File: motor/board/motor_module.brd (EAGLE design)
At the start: 44.4 x 51.7 mm, 74 parts, among them IC6 LTC6088, IC7 DRV8833RTY

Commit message: Added parallel pull-up to status
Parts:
- added R39: 4.7k, biomimetic:0402-RES
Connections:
- net SWD_DIO/STATUS: now also R39.1
- net V_3.0: now also R39.2
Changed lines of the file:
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@@
 <element name="R38" library="biomimetic" package="0402-RES" value="4.7k" x="20.32" y="10.16" rot="R180"/>
 <element name="C11" library="biomimetic" package="0402-CAP" value="100nF" x="10.16" y="29.21" rot="R270"/>
+<element name="R39" library="biomimetic" package="0402-RES" value="4.7k" x="-8.89" y="-3.81"/>
 </elements>
 <signals>
@@
 <contactref element="IC6" pad="4"/>
 <contactref element="C29" pad="1"/>
+<contactref element="R39" pad="2"/>
 <wire x1="27.94" y1="27.1526" x2="30.2" y2="26.92" width="0" layer="19" extent="1-1"/>
 <wire x1="30.23" y1="11.92" x2="30.2" y2="26.92" width="0" layer="19" extent="1-1"/>
@@
 <wire x1="8.47" y1="31.13" x2="8.4074" y2="20.32" width="0" layer="19" extent="1-1"/>
 <wire x1="10.16" y1="32.2326" x2="8.47" y2="31.13" width="0" layer="19" extent="1-1"/>
+<wire x1="-8.4074" y1="-3.81" x2="12.2174" y2="1.27" width="0" layer="19" extent="1-1"/>
 </signal>
 <signal name="V_1.5">
@@
 <contactref element="U$20" pad="24"/>
 <contactref element="STATUS_LED" pad="C"/>
+<contactref element="R39" pad="1"/>
 <wire x1="23.61" y1="8.89" x2="28.43" y2="12.72" width="0" layer="19" extent="1-1"/>
+<wire x1="-9.3726" y1="-3.81" x2="23.61" y2="8.89" width="0" layer="19" extent="1-1"/>
 </signal>
 <signal name="I2C_SCL">

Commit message: Moved pullup on charge management status to vbus
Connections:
- net V_3.0: no longer R6.1
- net V_BUS: now also R6.1
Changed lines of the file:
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@@
 <contactref element="C1" pad="1"/>
 <contactref element="U$1" pad="6"/>
-<wire x1="14.72" y1="7.62" x2="19.8374" y2="3.81" width="0" layer="19" extent="1-1"/>
-<wire x1="13.22" y1="7.62" x2="14.72" y2="7.62" width="0" layer="19" extent="1-1"/>
-<wire x1="11.43" y1="8.1026" x2="13.22" y2="7.62" width="0" layer="19" extent="1-1"/>
+<contactref element="R6" pad="1"/>
+<wire x1="6.67" y1="15.204" x2="8.4074" y2="20.32" width="0" layer="19" extent="1-1"/>
+<wire x1="5.8674" y1="12.7" x2="6.67" y2="15.204" width="0" layer="19" extent="1-1"/>
+<wire x1="2.54" y1="16.18" x2="6.67" y2="15.204" width="0" layer="19" extent="1-1"/>
+<wire x1="11.43" y1="8.1026" x2="5.8674" y2="12.7" width="0" layer="19" extent="1-1"/>
+<wire x1="13.22" y1="7.62" x2="11.43" y2="8.1026" width="0" layer="19" extent="1-1"/>
+<wire x1="14.72" y1="7.62" x2="13.22" y2="7.62" width="0" layer="19" extent="1-1"/>
 <wire x1="6.35" y1="4.81" x2="11.43" y2="8.1026" width="0" layer="19" extent="1-1"/>
-<wire x1="5.8674" y1="12.7" x2="11.43" y2="8.1026" width="0" layer="19" extent="1-1"/>
-<wire x1="6.67" y1="15.204" x2="5.8674" y2="12.7" width="0" layer="19" extent="1-1"/>
-<wire x1="2.54" y1="16.18" x2="6.67" y2="15.204" width="0" layer="19" extent="1-1"/>
+<wire x1="19.8374" y1="3.81" x2="14.72" y2="7.62" width="0" layer="19" extent="1-1"/>
 </signal>
 <signal name="N$4">
@@
 </signal>
 <signal name="V_3.0">
-<contactref element="R6" pad="1"/>
 <contactref element="C2" pad="1"/>
 <contactref element="U$11" pad="3"/>
@@
 <wire x1="13.4874" y1="3.81" x2="12.2174" y2="5.08" width="0" layer="19" extent="1-1"/>
 <wire x1="12.2174" y1="1.27" x2="13.4874" y2="3.81" width="0" layer="19" extent="1-1"/>
-<wire x1="8.4074" y1="20.32" x2="13.22" y2="7.22" width="0" layer="19" extent="1-1"/>
-<wire x1="8.47" y1="31.13" x2="8.4074" y2="20.32" width="0" layer="19" extent="1-1"/>
-<wire x1="10.16" y1="32.2326" x2="8.47" y2="31.13" width="0" layer="19" extent="1-1"/>
+<wire x1="10.16" y1="32.2326" x2="27.94" y2="27.1526" width="0" layer="19" extent="1-1"/>
+<wire x1="8.47" y1="31.13" x2="10.16" y2="32.2326" width="0" layer="19" extent="1-1"/>
 <wire x1="-8.4074" y1="-3.81" x2="12.2174" y2="1.27" width="0" layer="19" extent="1-1"/>
 </signal>

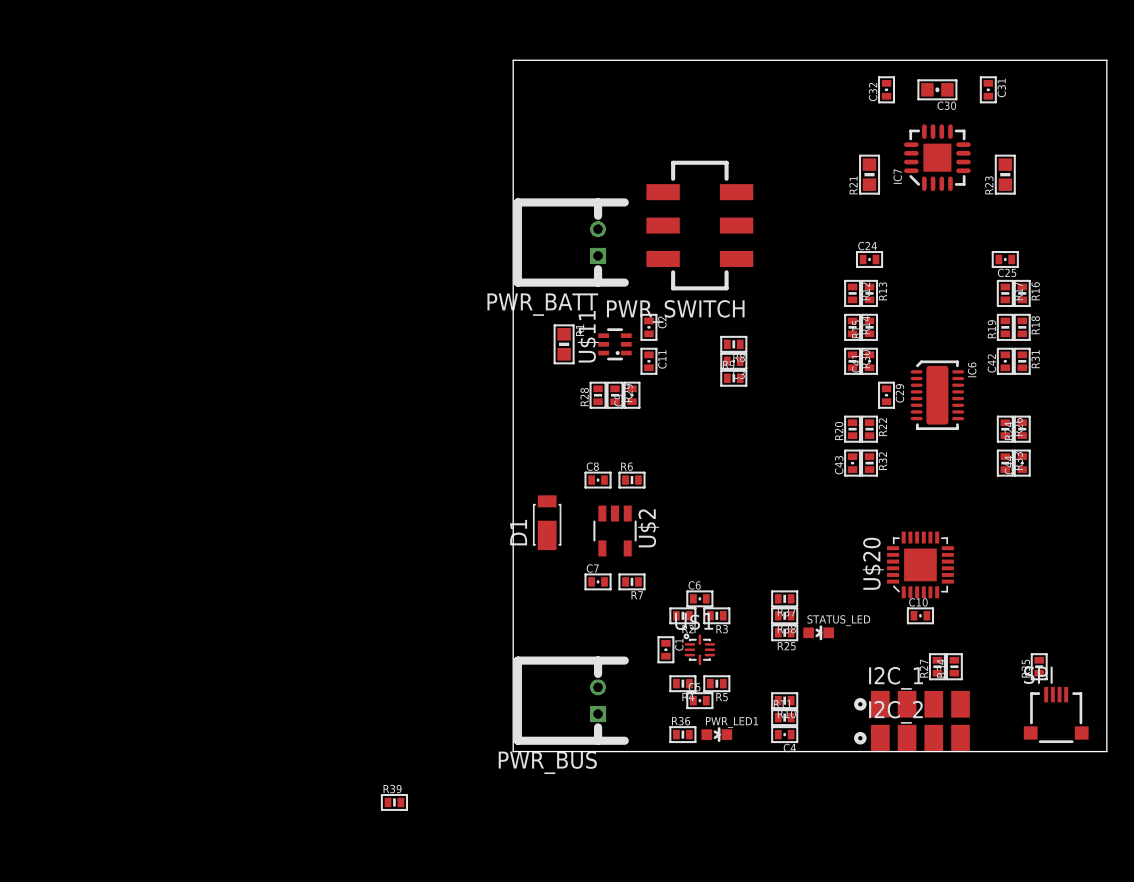
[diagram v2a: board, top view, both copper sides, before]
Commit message: Working on motor layout for modular motor driver
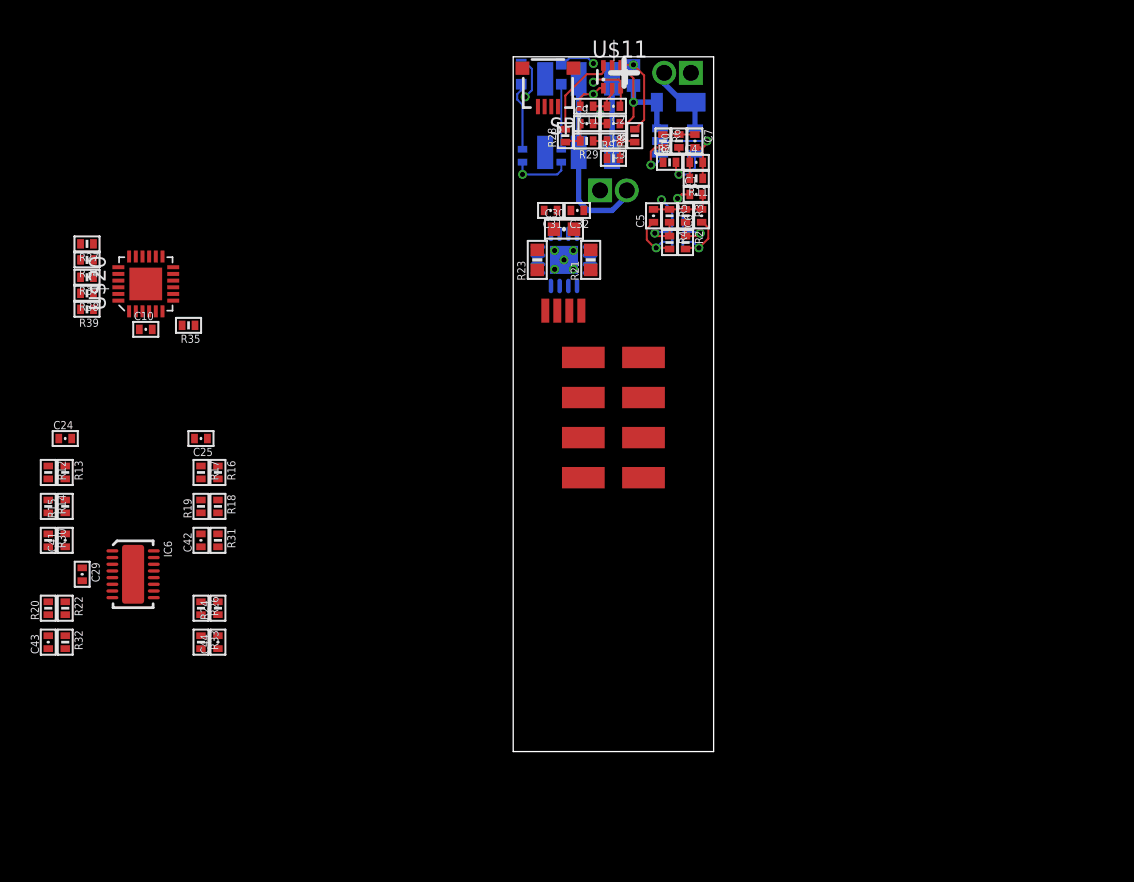
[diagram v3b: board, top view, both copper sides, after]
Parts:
- removed I2C_1, I2C_2: (no value), modular_robotics:1X04_2MM_BOARDEDGE
- added MA1, MA2, MB1, MB2: PAD-0.6_1.8, modular_robotics:PAD_0.6_1.8
- added U$27: MOTOR_HOUSING, modular_robotics:MOTOR_HOUSING
- PWR_BATT, PWR_BUS: value JST-RCY-FEMALE -> JST-RCY-FEMALEBATTERY; device modular_robotics:JST_2_FEMALE -> modular_robotics:TP_LIPO_160MAH
- moved R34 71.7 mm to (-31.9, 36.8), turned to 180 degrees
- moved R27 71.1 mm to (-31.9, 38.0), turned to 180 degrees
- moved R35 68.6 mm to (-24.3, 31.9), turned to 180 degrees
- moved C10 61.8 mm to (-27.5, 31.6)
- moved U$20 61.7 mm to (-27.5, 35.0)
- moved C24 61.7 mm to (-33.5, 23.4)
- moved C25 61.7 mm to (-23.4, 23.4)
- moved C29 61.7 mm to (-32.3, 13.3)
- moved C41 61.7 mm to (-33.5, 15.8)
- moved C42 61.7 mm to (-23.4, 15.8)
- moved C44 61.7 mm to (-22.1, 8.19)
- moved IC6 61.7 mm to (-28.4, 13.3)
- moved R13 61.7 mm to (-33.5, 20.9)
- moved R15 61.7 mm to (-33.5, 18.4)
- moved R16 61.7 mm to (-22.1, 20.9)
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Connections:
- net GND: now also PWR_BATT.V-, PWR_BUS.V-, U$27.2, U$27.6; no longer I2C_1.2, I2C_2.2, PWR_BATT.1, PWR_BUS.1
- net I2C_SCL: now also U$27.3, U$27.7; no longer I2C_1.3, I2C_2.3
- net I2C_SDA: now also U$27.4, U$27.8; no longer I2C_1.4, I2C_2.4
- net MOTOR_A_OUT1: now also MA1.1
- net MOTOR_A_OUT2: now also MA2.1
- net MOTOR_B_OUT1: now also MB1.1
- net MOTOR_B_OUT2: now also MB2.1
- net N$1: now also PWR_BATT.V+; no longer PWR_BATT.2
- net V_3.0: now also U$27.1, U$27.5; no longer I2C_1.1, I2C_2.1
- net V_BUS: now also PWR_BUS.V+; no longer PWR_BUS.2
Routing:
- net GND: track 0.00 -> 26.3 mm, vias 0 -> 9
- net I_BATT: track 0.00 -> 14.6 mm, vias 0 -> 1
- net N$1: track 0.00 -> 13.9 mm
- net V_3.0: track 0.00 -> 13.6 mm, vias 0 -> 3
- net V_BUS: track 0.00 -> 12.1 mm, vias 0 -> 1
- net V_BATT: track 0.00 -> 11.5 mm, vias 0 -> 1
- net V_1.5: track 0.00 -> 7.69 mm, vias 0 -> 2
- net N$6: track 0.00 -> 6.59 mm
- net N$7: track 0.00 -> 5.30 mm
- net N$8: track 0.00 -> 4.87 mm
- net N$4: track 0.00 -> 3.45 mm, vias 0 -> 1
- net CHARGE_STATUS: track 0.00 -> 3.34 mm, vias 0 -> 1
- net N$3: track 0.00 -> 3.22 mm, vias 0 -> 1
- net N$2: track 0.00 -> 3.22 mm, vias 0 -> 1
- net SENSE_V_BUS: track 0.00 -> 2.95 mm
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- added copper zone on layer 2, net GND
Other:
- board size 44.4 x 51.7 mm -> 15 x 52 mm

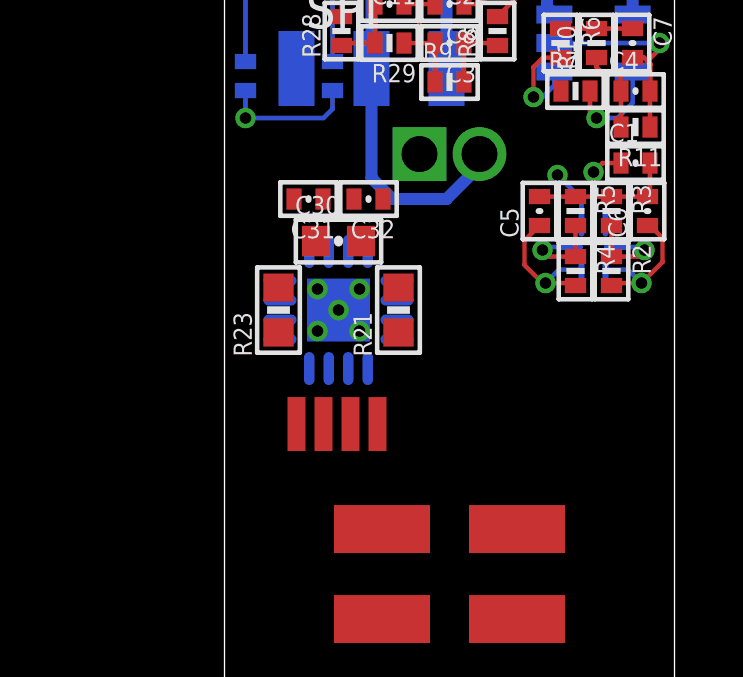
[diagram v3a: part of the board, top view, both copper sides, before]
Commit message: Motor driver laid out
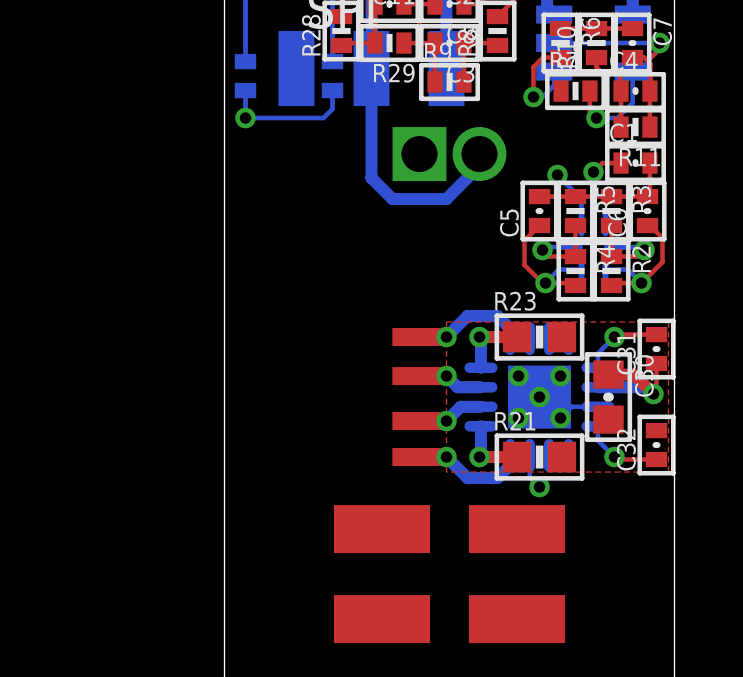
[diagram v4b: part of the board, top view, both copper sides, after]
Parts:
- moved C31 12.6 mm to (14.4, 35.5), turned to 90 degrees
- moved C32 12.6 mm to (14.4, 32.3), turned to 90 degrees
- moved C30 10.4 mm to (12.8, 33.9), turned to 270 degrees
- moved R23 8.75 mm to (10.5, 35.9), turned to 0 degrees
- moved IC7 7.30 mm to (10.5, 33.9), turned to 180 degrees
- moved R21 6.79 mm to (10.5, 31.9), turned to 0 degrees
- moved MB1 5.02 mm to (6.50, 35.9), turned to 270 degrees
- moved MB2 3.58 mm to (6.50, 34.6), turned to 270 degrees
- moved MA2 2.30 mm to (6.50, 33.1), turned to 270 degrees
- moved MA1 1.78 mm to (6.50, 31.9), turned to 270 degrees
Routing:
- net V_BATT: track 11.5 -> 17.4 mm, vias 1 -> 3
- net MOTOR_B_OUT1: track 0.00 -> 3.82 mm, vias 0 -> 1
- net MOTOR_A_OUT1: track 0.00 -> 3.82 mm, vias 0 -> 1
- net N$5: track 0.00 -> 2.69 mm, vias 0 -> 1
- net N$18: track 0.00 -> 2.69 mm, vias 0 -> 1
- net MOTOR_B_ISEN: track 0.00 -> 2.30 mm, vias 0 -> 1
- net MOTOR_A_ISEN: track 0.00 -> 2.30 mm, vias 0 -> 1
- net MOTOR_A_OUT2: track 0.00 -> 2.25 mm, vias 0 -> 1
- net MOTOR_B_OUT2: track 0.00 -> 2.21 mm, vias 0 -> 1
- net GND: track 26.3 -> 27.7 mm
- added copper zone on layer 1, net GND

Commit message: Working on final traces
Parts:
- moved R27 47.3 mm to (14.0, 26.5), turned to 0 degrees
- moved R37 47.3 mm to (14.0, 24.1), turned to 0 degrees
- moved R38 47.3 mm to (14.0, 22.9), turned to 0 degrees
- moved R39 47.3 mm to (14.0, 21.7), turned to 0 degrees
- moved R34 46.5 mm to (14.0, 29.5), turned to 0 degrees
- moved C29 43.9 mm to (5.20, 36.2), turned to 90 degrees
- moved R33 42.6 mm to (3.00, 41.7), turned to 90 degrees
- moved C43 41.5 mm to (1.80, 27.7)
- moved R32 41.4 mm to (3.00, 27.7)
- moved R20 41.2 mm to (1.80, 29.7)
- moved R22 41.2 mm to (3.00, 29.7)
- moved C44 41.2 mm to (1.80, 41.7), turned to 270 degrees
- moved R12 40.5 mm to (4.20, 31.7)
- moved R14 40.1 mm to (3.00, 31.7), turned to 90 degrees
- moved R30 39.9 mm to (1.80, 31.7)
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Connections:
- net MOTOR_B_ISEN: now also IC6.3; no longer IC6.12
- net N$26: now also IC6.2; no longer IC6.11
- net N$30: now also IC6.11; no longer IC6.2
- net N$31: now also IC6.12; no longer IC6.3
- net N$34: now also IC6.1; no longer IC6.10
- net N$36: now also IC6.10; no longer IC6.1
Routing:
- net V_3.0: track 13.6 -> 80.4 mm, vias 3 -> 7
- net V_BATT: track 17.4 -> 63.3 mm
- net V_1.5: track 7.69 -> 41.7 mm
- net SPI_SS: track 0.00 -> 31.4 mm, vias 0 -> 2
- net SPI_MISO: track 0.00 -> 28.5 mm, vias 0 -> 2
- net SPI_MOSI: track 0.00 -> 26.2 mm, vias 0 -> 2
- net SPI_SCK: track 0.00 -> 25.0 mm, vias 0 -> 2
- net GND: track 27.7 -> 48.9 mm, vias 9 -> 14
- net MOTOR_B_BEMF: track 0.00 -> 21.1 mm, vias 0 -> 3
- net I2C_SDA: track 0.00 -> 20.7 mm, vias 0 -> 1
- net SWD_DIO/STATUS: track 2.75 -> 15.4 mm
- net V_BUS: track 12.1 -> 24.4 mm, vias 1 -> 2
- net I2C_SCL: track 0.00 -> 12.2 mm, vias 0 -> 1
- net MOTOR_A_BEMF: track 0.00 -> 10.6 mm, vias 0 -> 1
- net MOTOR_A_IN1: track 0.00 -> 8.59 mm, vias 0 -> 1
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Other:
- board size 15 x 52 mm -> 15 x 52.5 mm

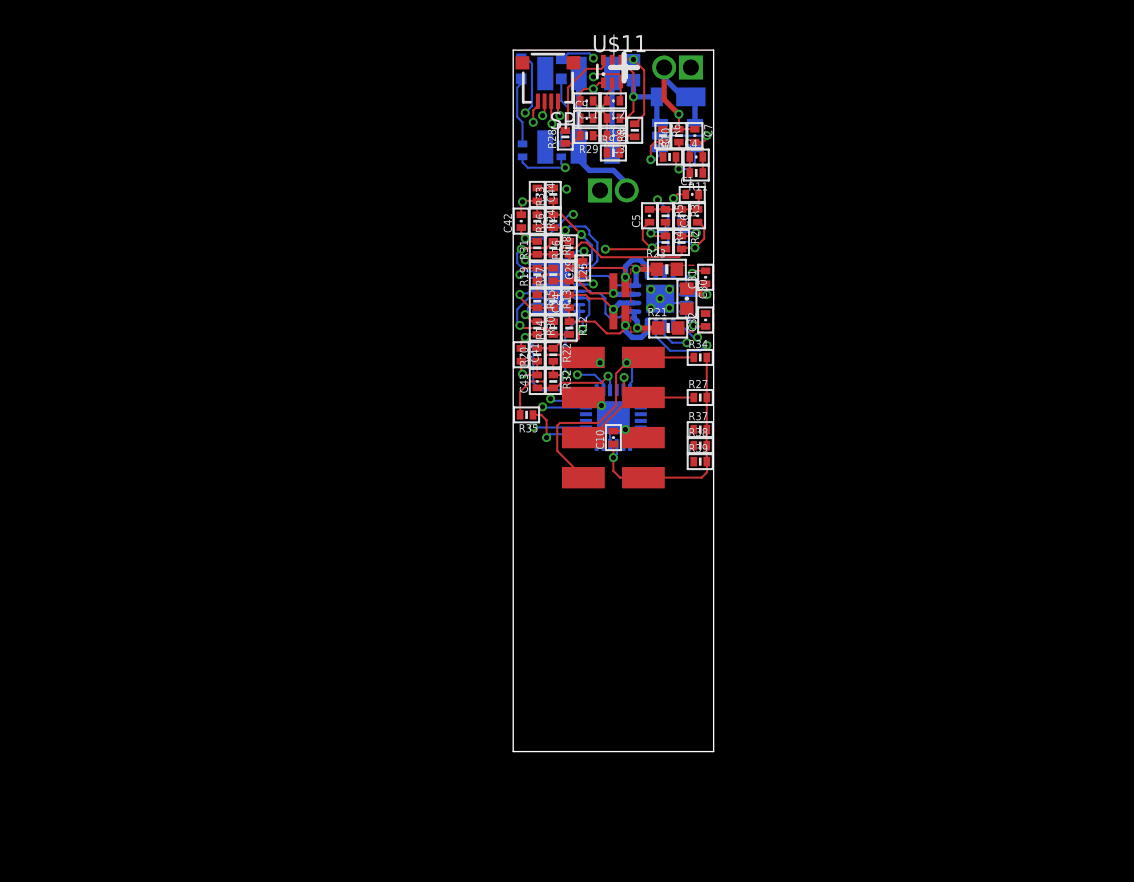
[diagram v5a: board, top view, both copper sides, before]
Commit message: Rough routing done, need to polish
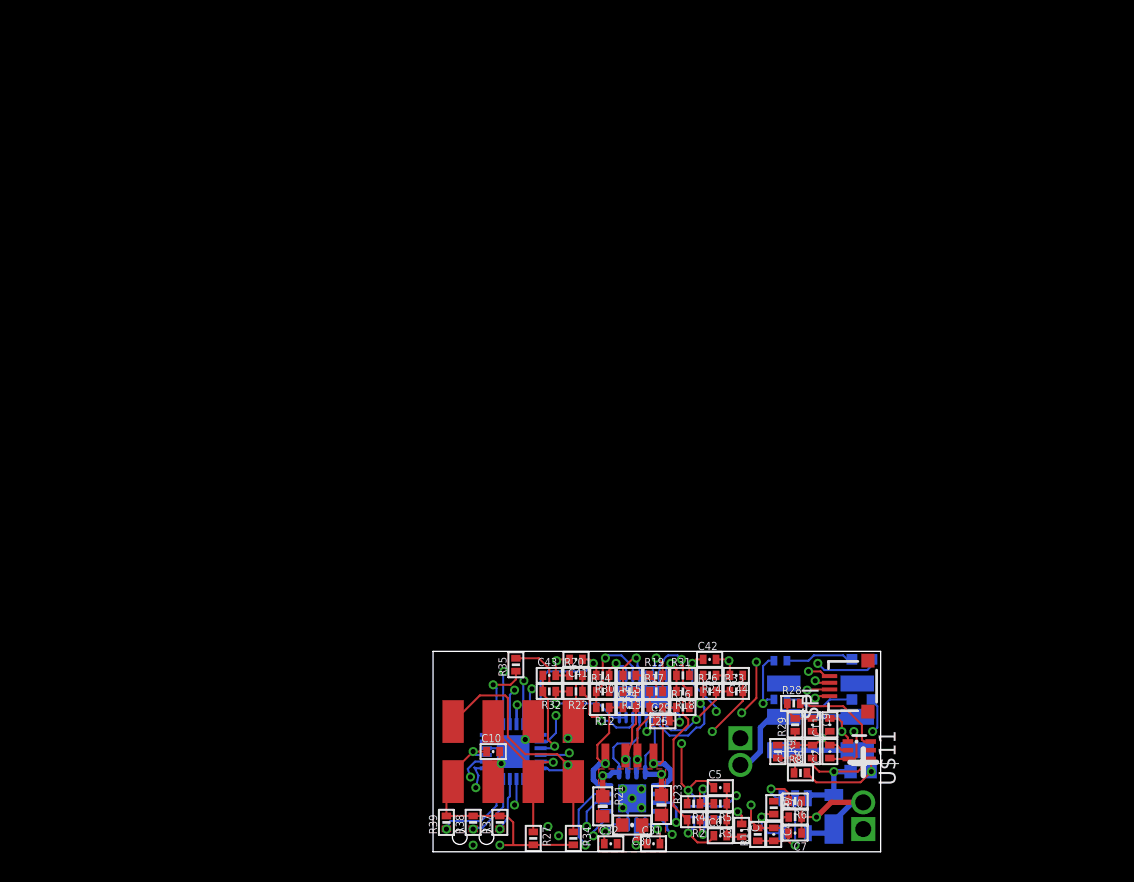
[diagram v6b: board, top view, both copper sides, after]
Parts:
- moved PWR_BUS 57.7 mm to (26.2, -4.80), turned to 270 degrees
- moved R1 55.2 mm to (26.0, -1.50), turned to 0 degrees
- moved D1 54.6 mm to (24.0, -4.20), turned to 90 degrees
- moved U$11 54.1 mm to (25.9, 0.10), turned to 270 degrees
- moved C7 52.7 mm to (21.1, -6.10), turned to 180 degrees
- moved STATUS_LED 52.3 mm to (26.1, 3.90), turned to 90 degrees
- moved R10 51.7 mm to (21.1, -4.90), turned to 0 degrees
- moved U$2 51.7 mm to (21.1, -4.80), turned to 180 degrees
- moved C2 51.3 mm to (23.7, 0.00), turned to 90 degrees
- moved C4 51.0 mm to (19.5, -6.20), turned to 270 degrees
- moved PWR_LED1 51.0 mm to (26.1, 6.90), turned to 90 degrees
- moved SPI 50.9 mm to (25.4, 4.90), turned to 90 degrees
- moved R6 50.8 mm to (21.1, -3.70), turned to 180 degrees
- moved C11 50.1 mm to (23.7, 2.00), turned to 90 degrees
- moved R11 49.7 mm to (18.3, -6.20), turned to 90 degrees
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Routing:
- net SWD_DIO/STATUS: track 15.4 -> 55.7 mm, vias 1 -> 4
- net MOTOR_B_IN2: track 0.00 -> 23.3 mm, vias 0 -> 2
- net SENSE_V_BUS: track 2.95 -> 25.3 mm, vias 0 -> 2
- net MOTOR_B_IN1: track 0.00 -> 21.3 mm, vias 0 -> 2
- net MOTOR_B_CURR: track 1.20 -> 19.5 mm, vias 1 -> 2
- net MOTOR_A_IN1: track 8.59 -> 19.9 mm, vias 1 -> 3
- net MOTOR_A_IN2: track 7.72 -> 17.4 mm, vias 1 -> 3
- net RESET: track 0.00 -> 5.01 mm, vias 0 -> 1
- net SWD_CLK: track 0.00 -> 3.99 mm, vias 0 -> 1
- net V_3.0: track 80.4 -> 81.8 mm, vias 7 -> 8
- net MOTOR_B_OUT2: track 7.06 -> 7.79 mm
- net V_1.5: track 41.7 -> 41.2 mm
- net GND: vias 14 -> 15
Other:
- board size 15 x 52.5 mm -> 33.5 x 15 mm
